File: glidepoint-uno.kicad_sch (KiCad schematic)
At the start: 8 parts, among them J1 Power, J2 Digital/PWM, J3 Analog, J4 Digital/PWM, J5 Conn_01x12_Socket, SW1 SW_Push, SW2 SW_Push

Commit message: Add 3 mounting holes.
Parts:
- added H1, H2, H3: MountingHole, mounting:MountingHole_M2_Pad_NonPTH_TopOnly, symbol Mechanical:MountingHole
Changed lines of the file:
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@@
+    )
+  )
+  (symbol (lib_id "Mechanical:MountingHole") (at 166.37 78.74 0) (unit 1)
+    (in_bom yes) (on_board yes) (dnp no) (fields_autoplaced)
+    (property "Reference" "H1" (at 168.91 77.47 0)
+      (effects (font (size 1.27 1.27)) (justify left))
+    )
+    (property "Value" "MountingHole" (at 168.91 80.01 0)
+      (effects (font (size 1.27 1.27)) (justify left))
+    )
+    (property "Footprint" "mounting:MountingHole_M2_Pad_NonPTH_TopOnly" (at 166.37 78.74 0)
+      (effects (font (size 1.27 1.27)) hide)
+    )
+    (property "Datasheet" "~" (at 166.37 78.74 0)
+      (effects (font (size 1.27 1.27)) hide)
+    )
+    (property "LCSC" "C2916319" (at 166.37 78.74 0)
+      (effects (font (size 1.27 1.27)) hide)
+    )
+    (instances
+      (project "glidepoint-uno"
+        (path "/e63e39d7-6ac0-4ffd-8aa3-1841a4541b55"
+          (reference "H1") (unit 1)
+        )
+      )
     )
   )
@@
     )
   )
+  (symbol (lib_id "Mechanical:MountingHole") (at 166.37 86.36 0) (unit 1)
+    (in_bom yes) (on_board yes) (dnp no) (fields_autoplaced)
+    (property "Reference" "H2" (at 168.91 85.09 0)
+      (effects (font (size 1.27 1.27)) (justify left))
+    )
+    (property "Value" "MountingHole" (at 168.91 87.63 0)
+      (effects (font (size 1.27 1.27)) (justify left))
+    )
+    (property "Footprint" "mounting:MountingHole_M2_Pad_NonPTH_TopOnly" (at 166.37 86.36 0)
+      (effects (font (size 1.27 1.27)) hide)
+    )
+    (property "Datasheet" "~" (at 166.37 86.36 0)
+      (effects (font (size 1.27 1.27)) hide)
+    )
+    (property "LCSC" "C2916319" (at 166.37 86.36 0)
+      (effects (font (size 1.27 1.27)) hide)
+    )
+    (instances
+      (project "glidepoint-uno"
+        (path "/e63e39d7-6ac0-4ffd-8aa3-1841a4541b55"
+          (reference "H2") (unit 1)
+        )
+      )
+    )
+  )
   (symbol (lib_id "Switch:SW_Push") (at 85.09 107.95 0) (unit 1)
     (in_bom yes) (on_board yes) (dnp no) (fields_autoplaced)
@@
         )
       )
+    )
+  )
+  (symbol (lib_id "Mechanical:MountingHole") (at 166.37 93.98 0) (unit 1)
+    (in_bom yes) (on_board yes) (dnp no) (fields_autoplaced)
+    (property "Reference" "H3" (at 168.91 92.71 0)
+      (effects (font (size 1.27 1.27)) (justify left))
+    )
+    (property "Value" "MountingHole" (at 168.91 95.25 0)
+      (effects (font (size 1.27 1.27)) (justify left))
+    )
+    (property "Footprint" "mounting:MountingHole_M2_Pad_NonPTH_TopOnly" (at 166.37 93.98 0)
+      (effects (font (size 1.27 1.27)) hide)
+    )
+    (property "Datasheet" "~" (at 166.37 93.98 0)
+      (effects (font (size 1.27 1.27)) hide)
+    )
+    (property "LCSC" "C2916319" (at 166.37 93.98 0)
+      (effects (font (size 1.27 1.27)) hide)
+    )
+    (instances
+      (project "glidepoint-uno"
+        (path "/e63e39d7-6ac0-4ffd-8aa3-1841a4541b55"
+          (reference "H3") (unit 1)
+        )
+      )

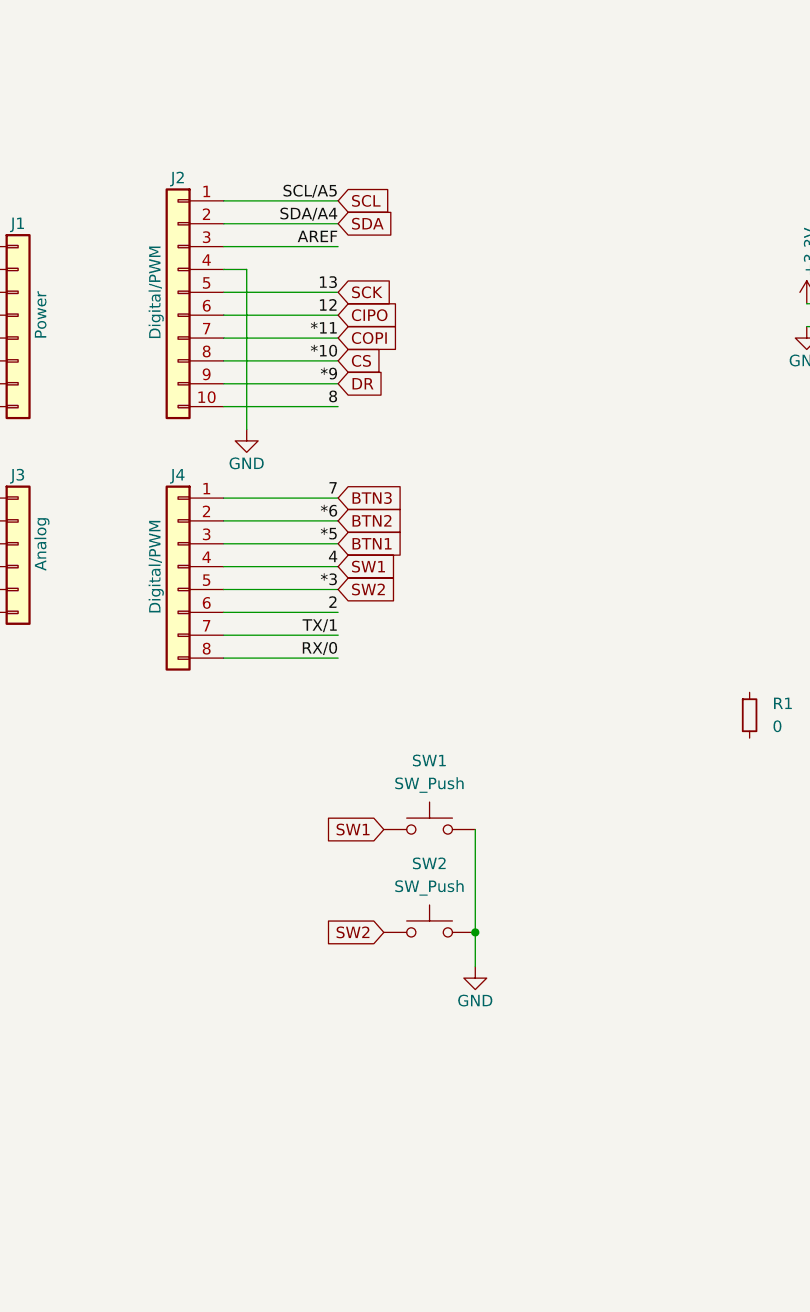
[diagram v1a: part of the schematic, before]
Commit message: Add i2c pull-ups, switch to Alps tactile buttons.
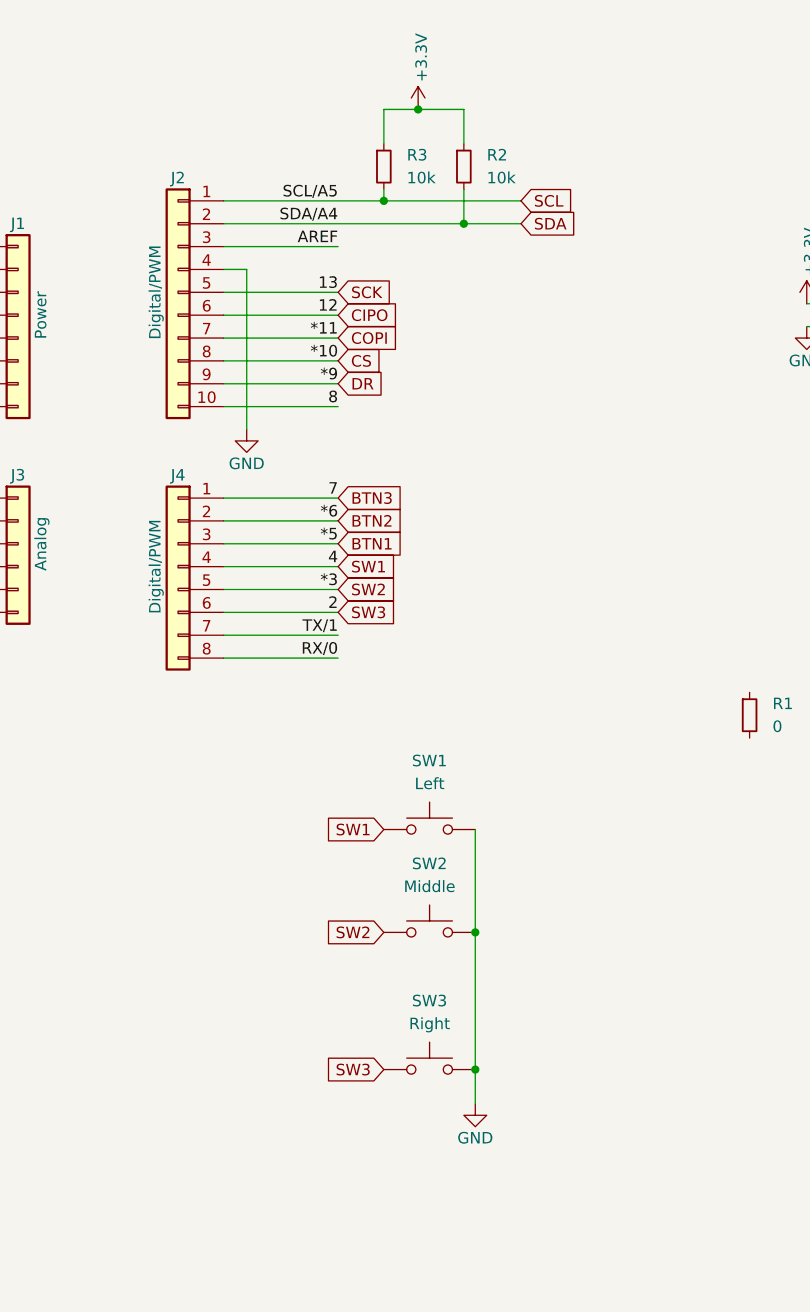
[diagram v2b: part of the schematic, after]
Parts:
- added R2, R3: 10k, Resistor_SMD:R_0805_2012Metric, symbol Device:R_Small
- added SW3: Right, buttons:SW_SKSTAAE010, symbol Switch:SW_Push
- SW1: value SW_Push -> Left; footprint mbk:Choc-1u -> buttons:SW_SKSTAAE010; LCSC C5333465 -> C202379
- SW2: value SW_Push -> Middle; footprint mbk:Choc-1u -> buttons:SW_SKSTAAE010; LCSC C5333465 -> C202379
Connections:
- net +3V3: now also R2.1, R3.1
- net GND: now also SW3.2
- net SCL: now also R3.2
- net SDA: now also R2.2
- net 2 renamed SW3
- net SW3: now also SW3.1
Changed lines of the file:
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@@
     (date "mar. 31 mars 2015")
   )
+  (junction (at 80.01 26.67) (diameter 0) (color 0 0 0 0)
+  )
   (junction (at 31.75 46.99) (diameter 1.016) (color 0 0 0 0)
   )
   (junction (at 90.17 107.95) (diameter 0) (color 0 0 0 0)
+  )
+  (junction (at 90.17 123.19) (diameter 0) (color 0 0 0 0)
+  )
+  (junction (at 88.9 29.21) (diameter 0) (color 0 0 0 0)
+  )
+  (junction (at 83.82 16.51) (diameter 0) (color 0 0 0 0)
   )
   (no_connect (at 34.29 31.75))
@@
     (stroke (width 0) (type solid))
   )
-  (wire (pts (xy 62.23 26.67) (xy 74.93 26.67))
-    (stroke (width 0) (type solid))
+  (wire (pts (xy 62.23 26.67) (xy 80.01 26.67))
+    (stroke (width 0) (type solid))
+  )
+  (wire (pts (xy 80.01 20.32) (xy 80.01 16.51))
+    (stroke (width 0) (type default))
+  )
+  (wire (pts (xy 80.01 25.4) (xy 80.01 26.67))
+    (stroke (width 0) (type default))
   )
   (wire (pts (xy 31.75 44.45) (xy 31.75 46.99))
     (stroke (width 0) (type solid))
   )
+  (wire (pts (xy 88.9 29.21) (xy 95.25 29.21))
+    (stroke (width 0) (type solid))
+  )
   (wire (pts (xy 21.59 72.39) (xy 34.29 72.39))
     (stroke (width 0) (type solid))
@@
     (stroke (width 0) (type default))
   )
-  (wire (pts (xy 90.17 107.95) (xy 90.17 111.76))
+  (wire (pts (xy 88.9 16.51) (xy 88.9 20.32))
+    (stroke (width 0) (type default))
+  )
+  (wire (pts (xy 90.17 107.95) (xy 90.17 123.19))
     (stroke (width 0) (type default))
   )
@@
     (stroke (width 0) (type solid))
   )
+  (wire (pts (xy 80.01 16.51) (xy 83.82 16.51))
+    (stroke (width 0) (type default))
+  )
+  (wire (pts (xy 90.17 123.19) (xy 90.17 127))
+    (stroke (width 0) (type default))
+  )
   (wire (pts (xy 62.23 36.83) (xy 74.93 36.83))
     (stroke (width 0) (type solid))
@@
     (stroke (width 0) (type solid))
   )
+  (wire (pts (xy 80.01 26.67) (xy 95.25 26.67))
+    (stroke (width 0) (type solid))
+  )
   (wire (pts (xy 62.23 46.99) (xy 74.93 46.99))
     (stroke (width 0) (type solid))
   )
+  (wire (pts (xy 83.82 16.51) (xy 88.9 16.51))
+    (stroke (width 0) (type default))
+  )
   (wire (pts (xy 90.17 96.52) (xy 90.17 107.95))
     (stroke (width 0) (type default))
@@
     (stroke (width 0) (type solid))
   )
-  (wire (pts (xy 62.23 29.21) (xy 74.93 29.21))
+  (wire (pts (xy 88.9 25.4) (xy 88.9 29.21))
+    (stroke (width 0) (type default))
+  )
+  (wire (pts (xy 62.23 29.21) (xy 88.9 29.21))
     (stroke (width 0) (type solid))
   )
@@
     (effects (font (size 1.27 1.27)) (justify left bottom))
   )
+  (global_label "SW3" (shape input) (at 74.93 72.39 0) (fields_autoplaced)
+    (effects (font (size 1.27 1.27)) (justify left))
+    (property "Intersheetrefs" "${INTERSHEET_REFS}" (at 81.8013 72.39 0)
+      (effects (font (size 1.27 1.27)) (justify left) hide)
+    )
+  )
   (global_label "DR" (shape input) (at 74.93 46.99 0) (fields_autoplaced)
     (effects (font (size 1.27 1.27)) (justify left))
@@
     )
   )
-  (global_label "SDA" (shape input) (at 74.93 29.21 0) (fields_autoplaced)
-    (effects (font (size 1.27 1.27)) (justify left))
-    (property "Intersheetrefs" "${INTERSHEET_REFS}" (at 81.499 29.21 0)
+  (global_label "SDA" (shape input) (at 95.25 29.21 0) (fields_autoplaced)
+    (effects (font (size 1.27 1.27)) (justify left))
+    (property "Intersheetrefs" "${INTERSHEET_REFS}" (at 101.819 29.21 0)
       (effects (font (size 1.27 1.27)) (justify left) hide)
     )
@@
     )
   )
-  (global_label "SCL" (shape input) (at 74.93 26.67 0) (fields_autoplaced)
-    (effects (font (size 1.27 1.27)) (justify left))
-    (property "Intersheetrefs" "${INTERSHEET_REFS}" (at 81.4385 26.67 0)
+  (global_label "SCL" (shape input) (at 95.25 26.67 0) (fields_autoplaced)
+    (effects (font (size 1.27 1.27)) (justify left))
+    (property "Intersheetrefs" "${INTERSHEET_REFS}" (at 101.7585 26.67 0)
       (effects (font (size 1.27 1.27)) (justify left) hide)
     )
@@
     (property "Intersheetrefs" "${INTERSHEET_REFS}" (at 81.8013 69.85 0)
       (effects (font (size 1.27 1.27)) (justify left) hide)
+    )
+  )
+  (global_label "SW3" (shape input) (at 80.01 123.19 180) (fields_autoplaced)
+    (effects (font (size 1.27 1.27)) (justify right))
+    (property "Intersheetrefs" "${INTERSHEET_REFS}" (at 73.1387 123.19 0)
+      (effects (font (size 1.27 1.27)) (justify right) hide)
     )
   )
@@
     )
   )
+  (symbol (lib_id "power:+3V3") (at 83.82 16.51 0) (unit 1)
+    (in_bom yes) (on_board yes) (dnp no)
+    (property "Reference" "#PWR09" (at 83.82 20.32 0)
+      (effects (font (size 1.27 1.27)) hide)
+    )
+    (property "Value" "+3.3V" (at 84.201 13.462 90)
+      (effects (font (size 1.27 1.27)) (justify left))
+    )
+    (property "Footprint" "" (at 83.82 16.51 0)
+      (effects (font (size 1.27 1.27)))
+    )
+    (property "Datasheet" "" (at 83.82 16.51 0)
+      (effects (font (size 1.27 1.27)))
+    )
+    (pin "1")
+    (instances
+      (project "glidepoint-uno"
+        (path "/e63e39d7-6ac0-4ffd-8aa3-1841a4541b55"
+          (reference "#PWR09") (unit 1)
+        )
+      )
+    )
+  )
   (symbol (lib_id "power:VCC") (at 26.67 26.67 0) (unit 1)
     (in_bom yes) (on_board yes) (dnp no)
@@
         (path "/e63e39d7-6ac0-4ffd-8aa3-1841a4541b55"
           (reference "H1") (unit 1)
+        )
+      )
+    )
+  )
+  (symbol (lib_id "Device:R_Small") (at 88.9 22.86 0) (unit 1)
+    (in_bom yes) (on_board yes) (dnp no) (fields_autoplaced)
+    (property "Reference" "R2" (at 91.44 21.59 0)
+      (effects (font (size 1.27 1.27)) (justify left))
+    )
+    (property "Value" "10k" (at 91.44 24.13 0)
+      (effects (font (size 1.27 1.27)) (justify left))
+    )
+    (property "Footprint" "Resistor_SMD:R_0805_2012Metric" (at 88.9 22.86 0)
+      (effects (font (size 1.27 1.27)) hide)
+    )
+    (property "Datasheet" "~" (at 88.9 22.86 0)
+      (effects (font (size 1.27 1.27)) hide)
+    )
+    (pin "1")
+    (pin "2")
+    (instances
+      (project "glidepoint-uno"
+        (path "/e63e39d7-6ac0-4ffd-8aa3-1841a4541b55"
+          (reference "R2") (unit 1)
+        )
+      )
+    )
+  )
+  (symbol (lib_id "Device:R_Small") (at 80.01 22.86 0) (unit 1)
+    (in_bom yes) (on_board yes) (dnp no) (fields_autoplaced)
+    (property "Reference" "R3" (at 82.55 21.59 0)
+      (effects (font (size 1.27 1.27)) (justify left))
+    )
+    (property "Value" "10k" (at 82.55 24.13 0)
+      (effects (font (size 1.27 1.27)) (justify left))
+    )
+    (property "Footprint" "Resistor_SMD:R_0805_2012Metric" (at 80.01 22.86 0)
+      (effects (font (size 1.27 1.27)) hide)
+    )
+    (property "Datasheet" "~" (at 80.01 22.86 0)
+      (effects (font (size 1.27 1.27)) hide)
+    )
+    (pin "1")
+    (pin "2")
+    (instances
+      (project "glidepoint-uno"
+        (path "/e63e39d7-6ac0-4ffd-8aa3-1841a4541b55"
+          (reference "R3") (unit 1)
         )
       )
@@
       (effects (font (size 1.27 1.27)))
     )
-    (property "Value" "SW_Push" (at 85.09 91.44 0)
-      (effects (font (size 1.27 1.27)))
-    )
-    (property "Footprint" "mbk:Choc-1u" (at 85.09 91.44 0)
+    (property "Value" "Left" (at 85.09 91.44 0)
+      (effects (font (size 1.27 1.27)))
+    )
+    (property "Footprint" "buttons:SW_SKSTAAE010" (at 85.09 91.44 0)
       (effects (font (size 1.27 1.27)) hide)
     )
@@
       (effects (font (size 1.27 1.27)) hide)
     )
-    (property "LCSC" "C5333465" (at 85.09 96.52 0)
+    (property "LCSC" "C202379" (at 85.09 96.52 0)
       (effects (font (size 1.27 1.27)) hide)
     )
@@
     )
   )
-  (symbol (lib_id "power:GND") (at 90.17 111.76 0) (unit 1)
-    (in_bom yes) (on_board yes) (dnp no)
-    (property "Reference" "#PWR08" (at 90.17 118.11 0)
-      (effects (font (size 1.27 1.27)) hide)
-    )
-    (property "Value" "GND" (at 90.17 115.57 0)
-      (effects (font (size 1.27 1.27)))
-    )
-    (property "Footprint" "" (at 90.17 111.76 0)
-      (effects (font (size 1.27 1.27)))
-    )
-    (property "Datasheet" "" (at 90.17 111.76 0)
+  (symbol (lib_id "power:GND") (at 90.17 127 0) (unit 1)
+    (in_bom yes) (on_board yes) (dnp no)
+    (property "Reference" "#PWR08" (at 90.17 133.35 0)
+      (effects (font (size 1.27 1.27)) hide)
+    )
+    (property "Value" "GND" (at 90.17 130.81 0)
+      (effects (font (size 1.27 1.27)))
+    )
+    (property "Footprint" "" (at 90.17 127 0)
+      (effects (font (size 1.27 1.27)))
+    )
+    (property "Datasheet" "" (at 90.17 127 0)
       (effects (font (size 1.27 1.27)))
     )
@@
       (effects (font (size 1.27 1.27)))
     )
-    (property "Value" "SW_Push" (at 85.09 102.87 0)
-      (effects (font (size 1.27 1.27)))
-    )
-    (property "Footprint" "mbk:Choc-1u" (at 85.09 102.87 0)
+    (property "Value" "Middle" (at 85.09 102.87 0)
+      (effects (font (size 1.27 1.27)))
+    )
+    (property "Footprint" "buttons:SW_SKSTAAE010" (at 85.09 102.87 0)
       (effects (font (size 1.27 1.27)) hide)
     )
@@
       (effects (font (size 1.27 1.27)) hide)
     )
-    (property "LCSC" "C5333465" (at 85.09 107.95 0)
+    (property "LCSC" "C202379" (at 85.09 107.95 0)
       (effects (font (size 1.27 1.27)) hide)
     )
@@
         )
       )
+    )
+  )
+  (symbol (lib_id "Switch:SW_Push") (at 85.09 123.19 0) (unit 1)
+    (in_bom yes) (on_board yes) (dnp no) (fields_autoplaced)
+    (property "Reference" "SW3" (at 85.09 115.57 0)
+      (effects (font (size 1.27 1.27)))
+    )
+    (property "Value" "Right" (at 85.09 118.11 0)
+      (effects (font (size 1.27 1.27)))
+    )
+    (property "Footprint" "buttons:SW_SKSTAAE010" (at 85.09 118.11 0)
+      (effects (font (size 1.27 1.27)) hide)
+    )
+    (property "Datasheet" "~" (at 85.09 118.11 0)
+      (effects (font (size 1.27 1.27)) hide)
+    )
+    (property "LCSC" "C202379" (at 85.09 123.19 0)
+      (effects (font (size 1.27 1.27)) hide)
+    )
+    (pin "1")
+    (pin "2")
+    (instances
+      (project "glidepoint-uno"
+        (path "/e63e39d7-6ac0-4ffd-8aa3-1841a4541b55"
+          (reference "SW3") (unit 1)
+        )
+      )
